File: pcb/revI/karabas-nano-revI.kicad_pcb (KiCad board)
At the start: 2 copper layers, 99.6 x 99.6 mm, 159 parts, among them J1 USB_B_Micro, J10 PWR, J11 AVR ISP, J2 TAPE IN/OUT, J3 A/V, J4 BUS, J5 KEYBOARD, J6 BUS, J7 JTAG, J8 AVR ISP, J9 RGB, Q2 BC856, SW1 RESET, SW10 8, SW11 9, SW12 0, SW13 Q, SW14 A, SW15 CS, SW16 W, SW17 S, SW18 Z, SW19 E, SW2 NMI, SW20 D, SW21 X, SW22 R, SW23 F, SW24 C, SW25 T, SW26 G, SW27 V, SW28 Y, SW29 H, SW3 1, SW30 B, SW31 U, SW32 J, SW33 N, SW34 I, SW35 K, SW36 M, SW37 O, SW38 L, SW39 SS, SW4 2, SW40 P, SW41 Enter, SW42 Space, SW5 3, SW6 4, SW7 5, SW8 6, SW9 7, U1 Z80, U10 ATmega88, U13 1117-3.3, U2 39F040, U3 CY62167ELL, U4 ATmega88, U5 ESP-12E, U6 EPM3256ATC144, U7 MicroSD, U8 LM311, U9 AD724, Y1 28MHz, Y3 4.43MHz

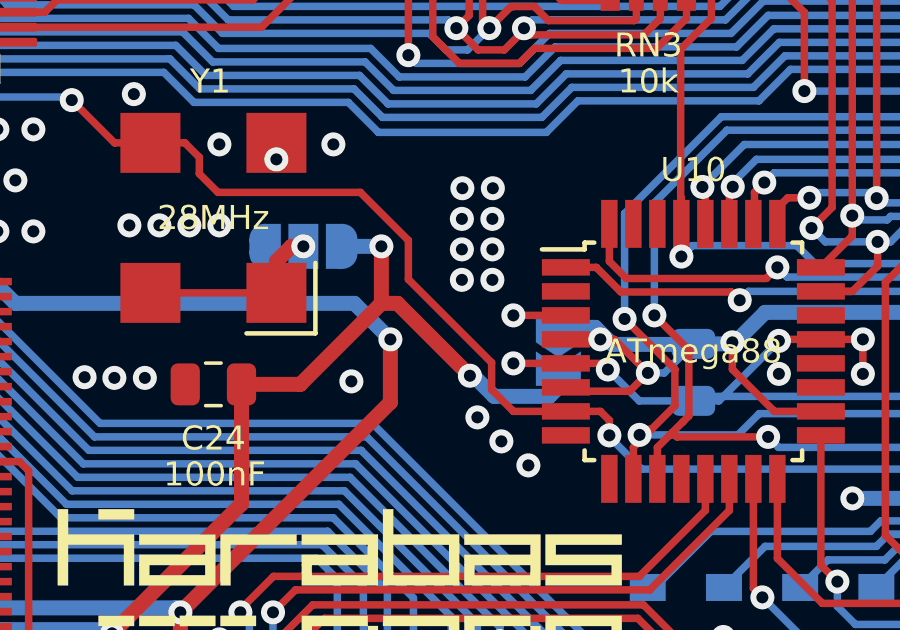
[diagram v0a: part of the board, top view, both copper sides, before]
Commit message: Updated 3d models on revI board
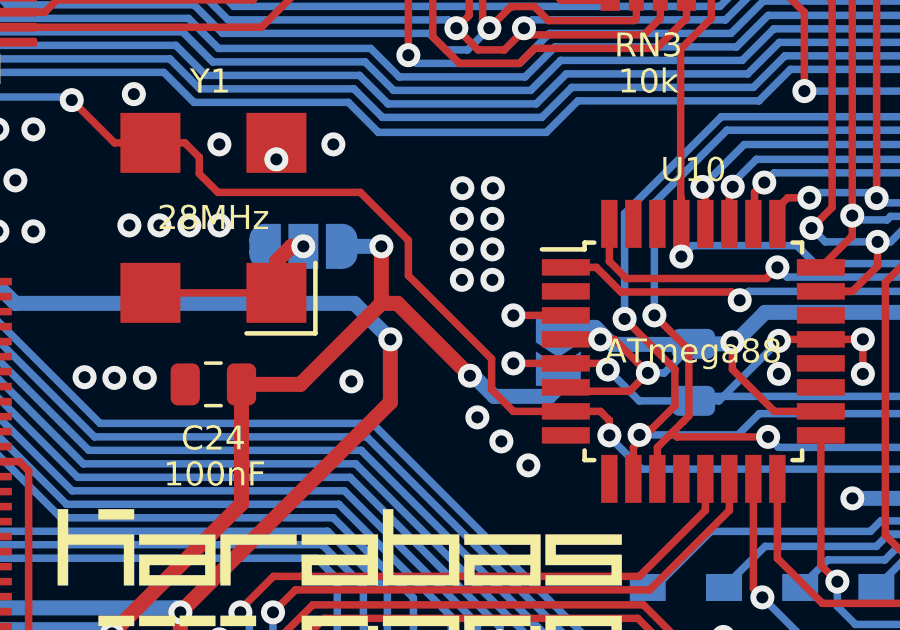
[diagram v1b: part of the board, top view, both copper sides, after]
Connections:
- net /~BTN_NMI renamed /~{BTN_NMI}
- net /~BUSACK renamed /~{BUSACK}
- net /~BUSREQ renamed /~{BUSREQ}
- net /~BUS_IORQGE renamed /~{BUS_IORQGE}
- net /~BUS_ROMCS renamed /~{BUS_ROMCS}
- net /~HALT renamed /~{HALT}
- net /~INT renamed /~{INT}
- net /~IORQ renamed /~{IORQ}
- net /~M1 renamed /~{M1}
- net /~MRD renamed /~{MRD}
- net /~MREQ renamed /~{MREQ}
- net /~MWR renamed /~{MWR}
- net /~NMI renamed /~{NMI}
- net /~RD renamed /~{RD}
- net /~RFSH renamed /~{RFSH}
- net /~ROMCS renamed /~{ROMCS}
- net /~ROM_WE renamed /~{ROM_WE}
- net /~SD_CS renamed /~{SD_CS}
- net /~WAIT renamed /~{WAIT}
- net /~WR renamed /~{WR}
- net ~RESET renamed ~{RESET}

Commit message: Small improvements: moved RN3 outside the plcc32 socket, rerouted vias under logo
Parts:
- moved RN3 3.12 mm to (157.5, 90.4), turned to 0 degrees
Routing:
- net GND: track 276.7 -> 297.5 mm, vias 376 -> 379
- net ~{RESET}: track 294.5 -> 291.5 mm, vias 18 -> 17
- net VCC: track 423.1 -> 425.9 mm
- net KB3: track 187.2 -> 189.8 mm
- net /KB5: track 67.4 -> 70.0 mm
- net /~{WAIT}: track 73.0 -> 70.4 mm
- net /AY_OUT_L: track 132.7 -> 135.0 mm
- net /AY_OUT_R: track 125.7 -> 128.0 mm
- net KB1: track 248.7 -> 250.8 mm
- net KB4: track 169.3 -> 171.3 mm
- net /AY_OUT_R2: track 113.2 -> 114.8 mm
- net KB2: track 210.4 -> 211.8 mm
- net /AY_OUT_L2: track 115.3 -> 116.6 mm
- net /~{BUSREQ}: track 92.2 -> 90.9 mm
- net /~{NMI}: track 64.7 -> 65.7 mm
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
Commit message: Changed  label due to PCBWay violations
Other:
- board text added: "Designed in Ukraine"
- board text removed: "Made in Ukraine"
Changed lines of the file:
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@@
-(kicad_pcb (version 20210623) (generator pcbnew)
+(kicad_pcb (version 20210722) (generator pcbnew)
   (general
     (thickness 1.6)
@@
   (gr_line (start 96.52 82.296) (end 96.52 92.964) (layer "F.Fab") (width 0.2))
   (gr_line (start 96.52 92.964) (end 92.456 92.964) (layer "F.Fab") (width 0.2))
-  (gr_text "Made in Ukraine" (at 181.864 147.574) (layer "B.SilkS")
+  (gr_text "Designed in Ukraine" (at 181.864 147.574) (layer "B.SilkS")
     (effects (font (size 1 1) (thickness 0.15)) (justify left mirror))
   )
